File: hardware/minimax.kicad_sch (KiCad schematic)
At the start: 0 parts

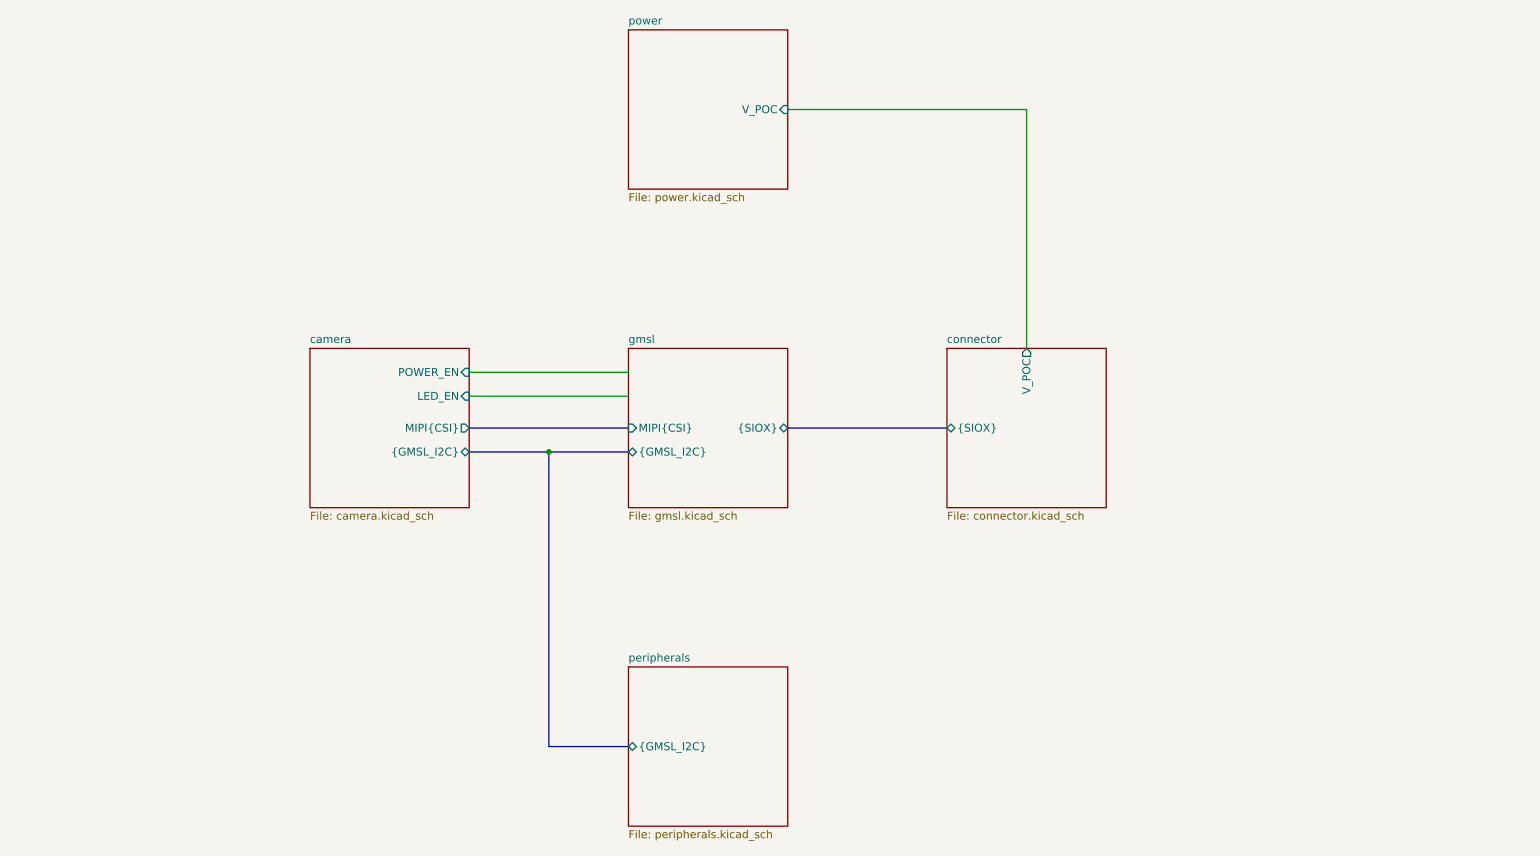
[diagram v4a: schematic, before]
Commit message: finished schematic, changed to 4 layer board
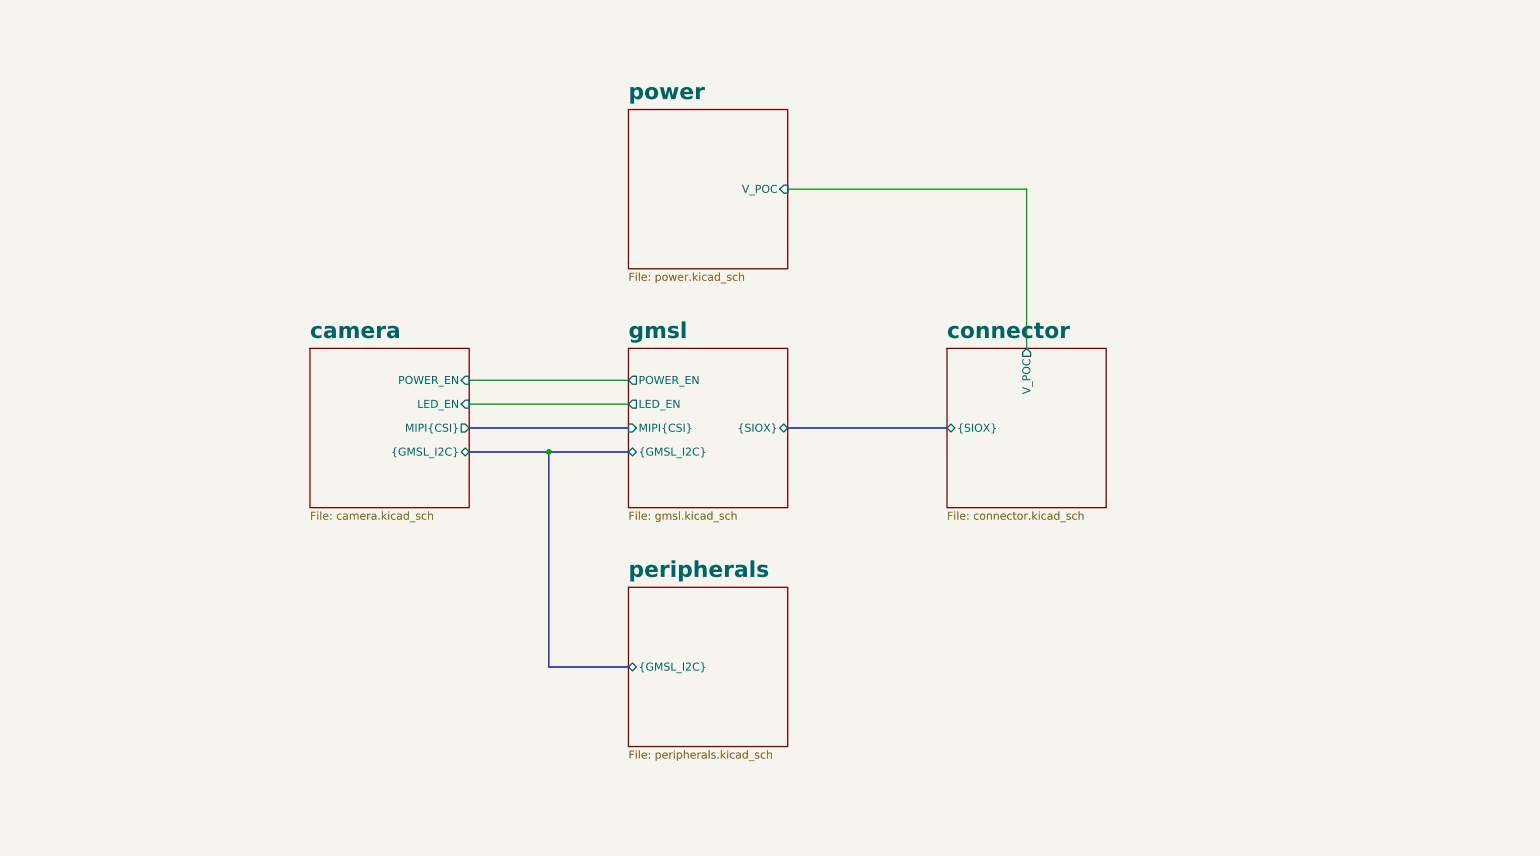
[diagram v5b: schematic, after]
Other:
- sheet gmsl ports: added LED_EN, POWER_EN; removed none
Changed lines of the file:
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@@
 	(wire
 		(pts
-			(xy 101.6 92.71) (xy 127 92.71)
+			(xy 101.6 93.98) (xy 127 93.98)
 		)
 		(stroke
@@
 	(bus
 		(pts
-			(xy 114.3 152.4) (xy 114.3 105.41)
+			(xy 114.3 139.7) (xy 114.3 105.41)
 		)
 		(stroke
@@
 	(bus
 		(pts
-			(xy 127 152.4) (xy 114.3 152.4)
+			(xy 127 139.7) (xy 114.3 139.7)
 		)
 		(stroke
@@
 	(wire
 		(pts
-			(xy 190.5 88.9) (xy 190.5 50.8)
+			(xy 190.5 88.9) (xy 190.5 63.5)
 		)
 		(stroke
@@
 	(wire
 		(pts
-			(xy 101.6 96.52) (xy 127 96.52)
+			(xy 101.6 97.79) (xy 127 97.79)
 		)
 		(stroke
@@
 	(wire
 		(pts
-			(xy 190.5 50.8) (xy 152.4 50.8)
-		)
-		(stroke
-			(width 0)
-			(type default)
-		)
-	)
-	(sheet
-		(at 127 139.7)
+			(xy 190.5 63.5) (xy 152.4 63.5)
+		)
+		(stroke
+			(width 0)
+			(type default)
+		)
+	)
+	(sheet
+		(at 127 127)
 		(size 25.4 25.4)
 		(fields_autoplaced yes)
@@
 		)
 		(property "Sheetname" "peripherals"
-			(at 127 138.9884 0)
-			(effects
-				(font
-					(size 1.27 1.27)
+			(at 127 125.6534 0)
+			(effects
+				(font
+					(size 2.54 2.54)
+					(thickness 0.508)
+					(bold yes)
 				)
 				(justify left bottom)
@@
 		)
 		(property "Sheetfile" "peripherals.kicad_sch"
-			(at 127 165.6846 0)
+			(at 127 152.9846 0)
 			(effects
 				(font
@@
 		)
 		(pin "{GMSL_I2C}" bidirectional
-			(at 127 152.4 180)
+			(at 127 139.7 180)
 			(effects
 				(font
@@
 		)
 		(property "Sheetname" "gmsl"
-			(at 127 88.1884 0)
-			(effects
-				(font
-					(size 1.27 1.27)
+			(at 127 87.5534 0)
+			(effects
+				(font
+					(size 2.54 2.54)
+					(thickness 0.508)
+					(bold yes)
 				)
 				(justify left bottom)
@@
 				)
 				(justify right)
+			)
+		)
+		(pin "POWER_EN" output
+			(at 127 93.98 180)
+			(effects
+				(font
+					(size 1.27 1.27)
+				)
+				(justify left)
+			)
+		)
+		(pin "LED_EN" output
+			(at 127 97.79 180)
+			(effects
+				(font
+					(size 1.27 1.27)
+				)
+				(justify left)
 			)
 		)
@@
 		)
 		(property "Sheetname" "connector"
-			(at 177.8 88.1884 0)
-			(effects
-				(font
-					(size 1.27 1.27)
+			(at 177.8 87.5534 0)
+			(effects
+				(font
+					(size 2.54 2.54)
+					(thickness 0.508)
+					(bold yes)
 				)
 				(justify left bottom)
@@
 		)
 		(property "Sheetname" "camera"
-			(at 76.2 88.1884 0)
-			(effects
-				(font
-					(size 1.27 1.27)
+			(at 76.2 87.5534 0)
+			(effects
+				(font
+					(size 2.54 2.54)
+					(thickness 0.508)
+					(bold yes)
 				)
 				(justify left bottom)
@@
 		)
 		(pin "POWER_EN" input
-			(at 101.6 92.71 0)
+			(at 101.6 93.98 0)
 			(effects
 				(font
@@
 		)
 		(pin "LED_EN" input
-			(at 101.6 96.52 0)
+			(at 101.6 97.79 0)
 			(effects
 				(font
@@
 	)
 	(sheet
-		(at 127 38.1)
+		(at 127 50.8)
 		(size 25.4 25.4)
 		(fields_autoplaced yes)
@@
 		)
 		(property "Sheetname" "power"
-			(at 127 37.3884 0)
-			(effects
-				(font
-					(size 1.27 1.27)
+			(at 127 49.4534 0)
+			(effects
+				(font
+					(size 2.54 2.54)
+					(thickness 0.508)
+					(bold yes)
 				)
 				(justify left bottom)
@@
 		)
 		(property "Sheetfile" "power.kicad_sch"
-			(at 127 64.0846 0)
+			(at 127 76.7846 0)
 			(effects
 				(font
@@
 		)
 		(pin "V_POC" input
-			(at 152.4 50.8 0)
-			(effects
-				(font
+			(at 152.4 63.5 0)
+			(effects
+				(font
